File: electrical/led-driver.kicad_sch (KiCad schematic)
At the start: 7 parts, among them J3 0705430001, Q2 AO3400A, U3 SN74LVC08ADR

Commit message: Continue layout...
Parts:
- J3: footprint Connector_PinHeader_2.54mm:PinHeader_1x02_P2.54mm_Vertical -> !Connectors:molex_0705430001
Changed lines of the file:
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@@
 			)
 		)
-		(property "Footprint" "Connector_PinHeader_2.54mm:PinHeader_1x02_P2.54mm_Vertical"
+		(property "Footprint" "!Connectors:molex_0705430001"
 			(at 168.91 76.2 0)
 			(effects

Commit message: Layout complete
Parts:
- J3: FT Rotation Offset (none) -> 90
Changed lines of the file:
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@@
+			)
+		)
+		(property "FT Rotation Offset" "90"
+			(at 168.91 76.2 0)
+			(effects
+				(font
+					(size 1.27 1.27)
+				)
+				(hide yes)
 			)
 		)

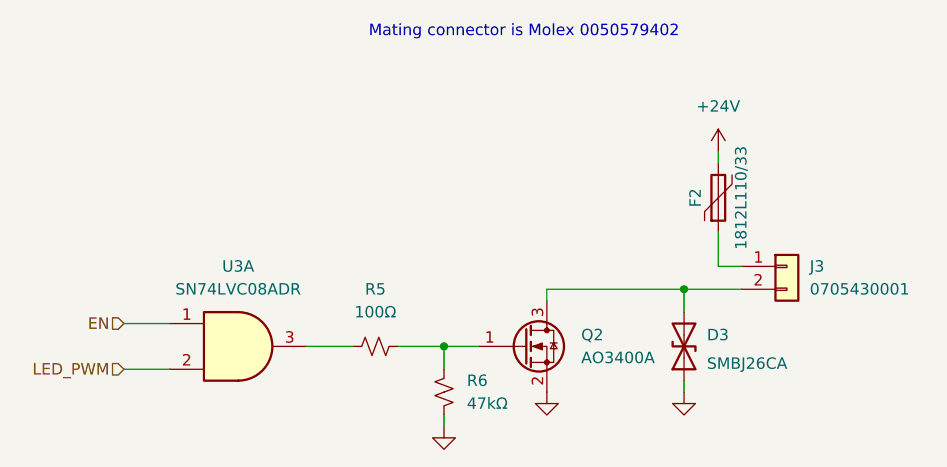
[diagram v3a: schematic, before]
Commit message: Finished and submitted to JLCPCB
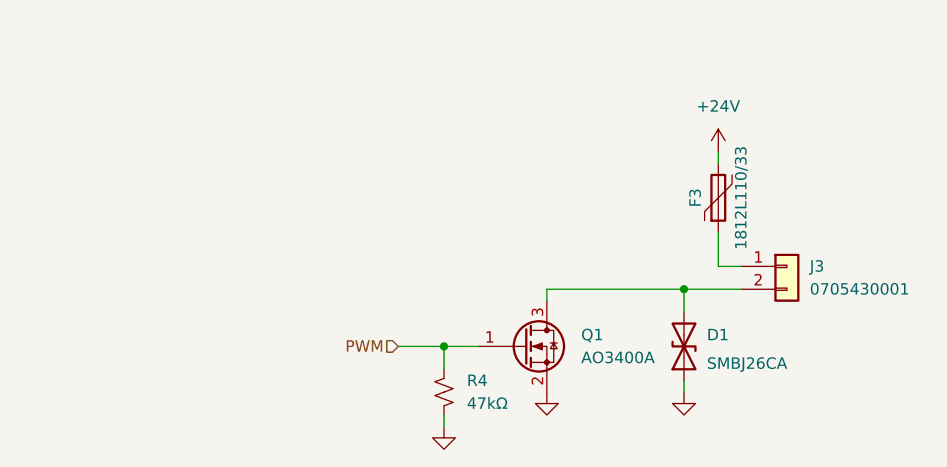
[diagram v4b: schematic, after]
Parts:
- removed R5: 100Ω, Resistor_SMD:R_0603_1608Metric, symbol !Resistor-0603:100Ω
- removed U3: SN74LVC08ADR, Package_SO:SOIC-14_3.9x8.7mm_P1.27mm, symbol !Logic-Buffer:74LVC08ADB
- Q1: renamed from Q2; DigiKey (none) -> 785-1000-1-ND
- renumbered D3 to D1, F2 to F3, R6 to R4
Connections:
- net PWM: now reaches Q1.1 (G), R4.1
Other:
- note removed: "Mating connector is Molex 0050579402"
